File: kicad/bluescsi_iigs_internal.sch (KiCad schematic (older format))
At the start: 23 parts, among them J1 Conn_02x13_Odd_Even, J2 Conn_02x13_Odd_Even, J3 105162-0001, J4 Conn_01x02_Male, SW1 SW_SPDT, U1 YAAJ_BluePill, U2 UCC5606, U3 UCC5606, U4 AMS1117-5.0

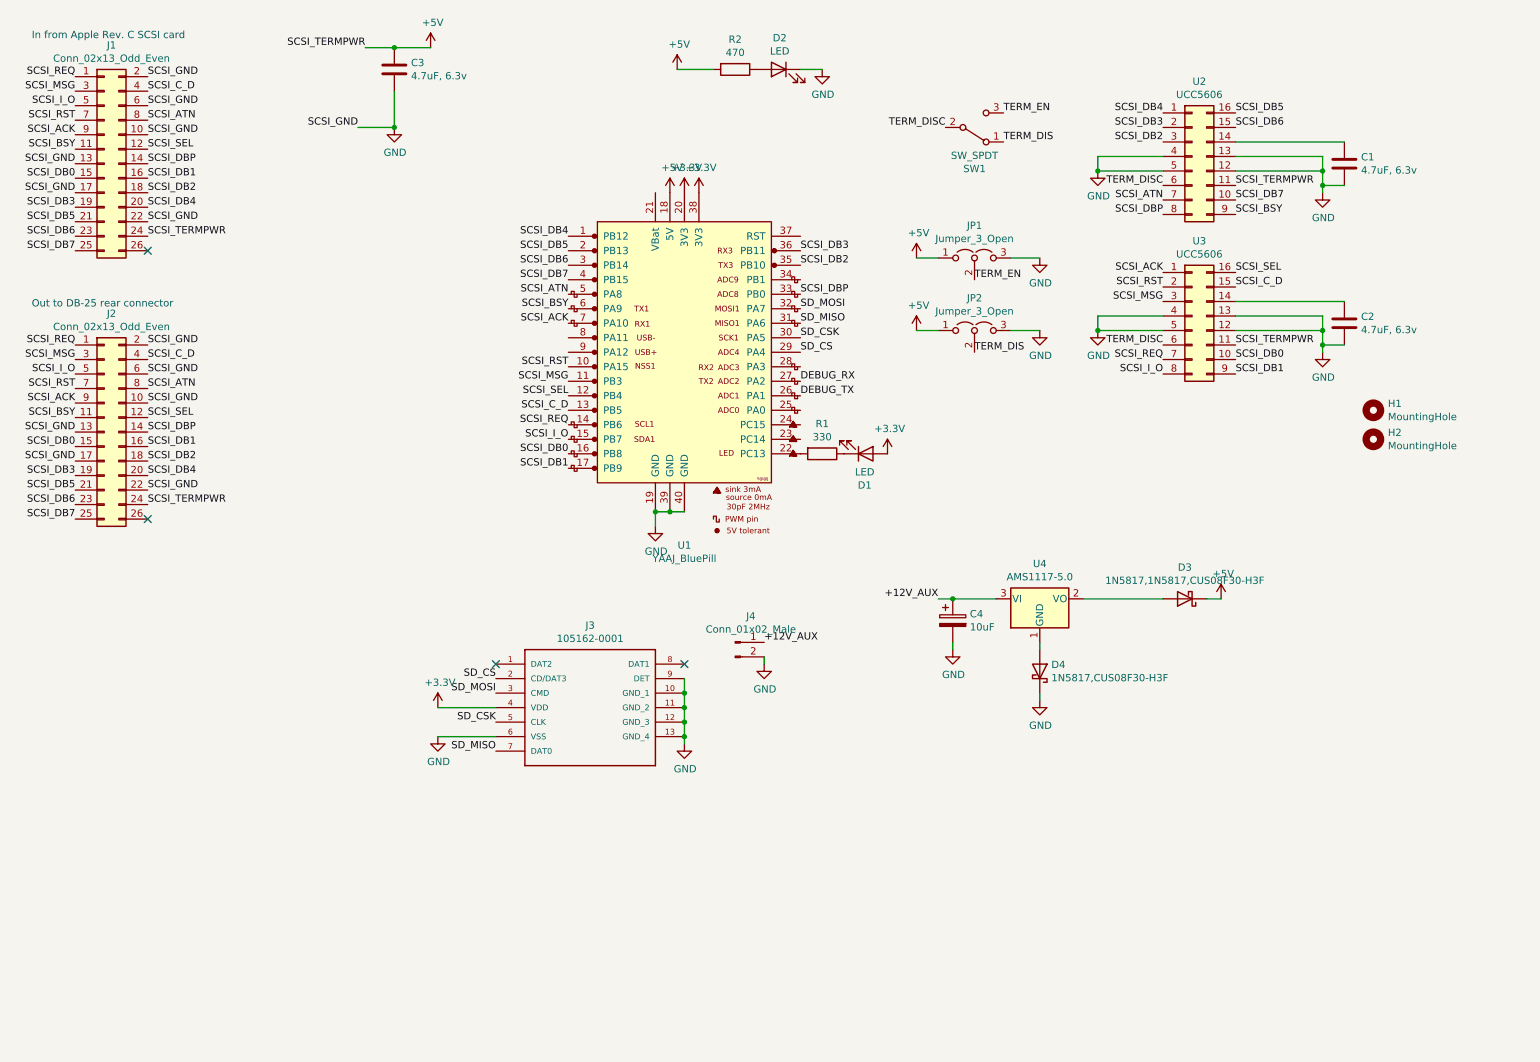
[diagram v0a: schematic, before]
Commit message: Updated schematic to group items and make them more readable
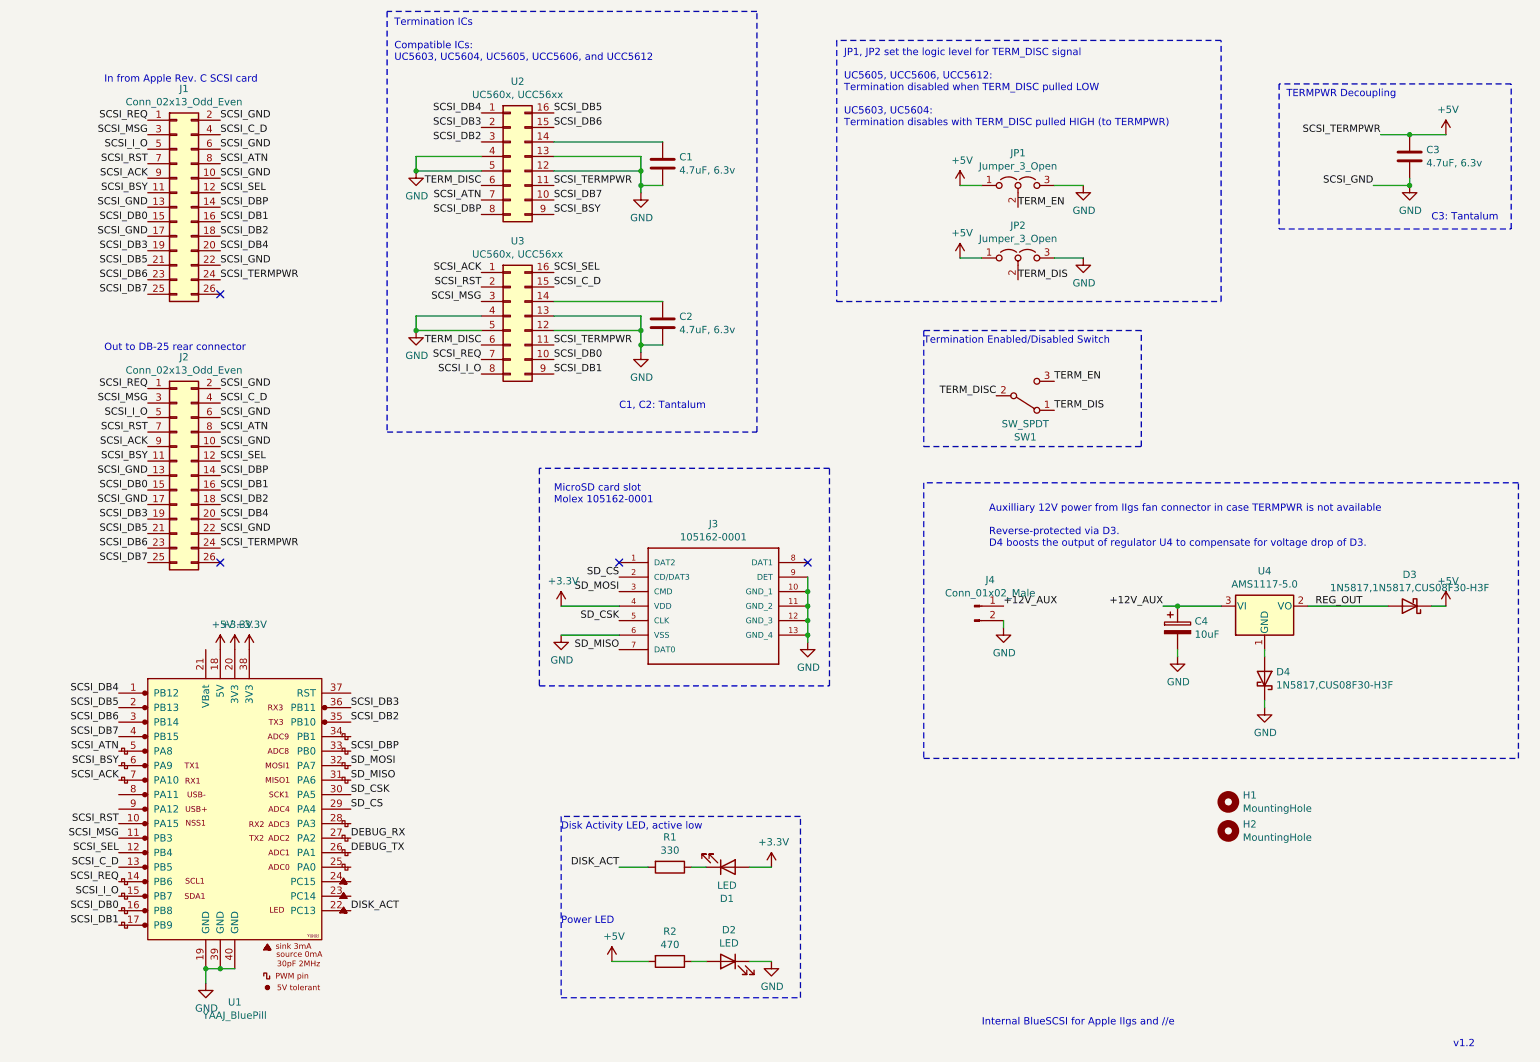
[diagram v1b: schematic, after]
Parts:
- U2, U3: value UCC5606 -> UC560x, UCC56xx
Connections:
- net DISK_ACT: now reaches R1.2, U1.22 (PC13)
- net REG_OUT: now reaches D3.2 (A), U4.2 (VO)
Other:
- note added: "Auxilliary 12V power from IIgs fan connector in case TERMPWR is not available\n\nReverse-protected via D3.\nD4 boosts the output of regulator U4 to compensate for voltage drop of D3."
- note added: "C1, C2: Tantalum"
- note added: "C3: Tantalum"
- note added: "Disk Activity LED, active low"
- note added: "Internal BlueSCSI for Apple IIgs and //e"
- note added: "JP1, JP2 set the logic level for TERM_DISC signal\n\nUC5605, UCC5606, UCC5612:\nTermination disabled when TERM_DISC pulled LOW\n\nUC5603, UC5604:\nTermination disables with TERM_DISC pulled HIGH (to TERMPWR)"
- note added: "MicroSD card slot\nMolex 105162-0001"
- note added: "Power LED"
- note added: "TERMPWR Decoupling"
- note added: "Termination Enabled/Disabled Switch"
- note added: "Termination ICs\n\nCompatible ICs:\nUC5603, UC5604, UC5605, UCC5606, and UCC5612"
- note added: "v1.2"
- moved on the sheet: C1, C2, C3, C4, D1, D2, D3, D4, H1, H2, J1, J2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

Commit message: Update notes about which JP setting to use with UCC5612
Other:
- note added: "JP1, JP2 set the logic level for TERM_DISC signal\n\nUC5605, UCC5606:\nTermination disabled when TERM_DISC pulled LOW\n\nUC5603, UC5604, UCC5612:\nTermination disables with TERM_DISC pulled HIGH (to TERMPWR)"
- note removed: "JP1, JP2 set the logic level for TERM_DISC signal\n\nUC5605, UCC5606, UCC5612:\nTermination disabled when TERM_DISC pulled LOW\n\nUC5603, UC5604:\nTermination disables with TERM_DISC pulled HIGH (to TERMPWR)"
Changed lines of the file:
@@
 Termination ICs\n\nCompatible ICs:\nUC5603, UC5604, UC5605, UCC5606, and UCC5612
 Text Notes 6400 1300 0    50   ~ 0
-JP1, JP2 set the logic level for TERM_DISC signal\n\nUC5605, UCC5606, UCC5612:\nTermination disabled when TERM_DISC pulled LOW\n\nUC5603, UC5604:\nTermination disables with TERM_DISC pulled HIGH (to TERMPWR)
+JP1, JP2 set the logic level for TERM_DISC signal\n\nUC5605, UCC5606:\nTermination disabled when TERM_DISC pulled LOW\n\nUC5603, UC5604, UCC5612:\nTermination disables with TERM_DISC pulled HIGH (to TERMPWR)
 Text Notes 6950 2800 0    50   ~ 0
 Termination Enabled/Disabled Switch

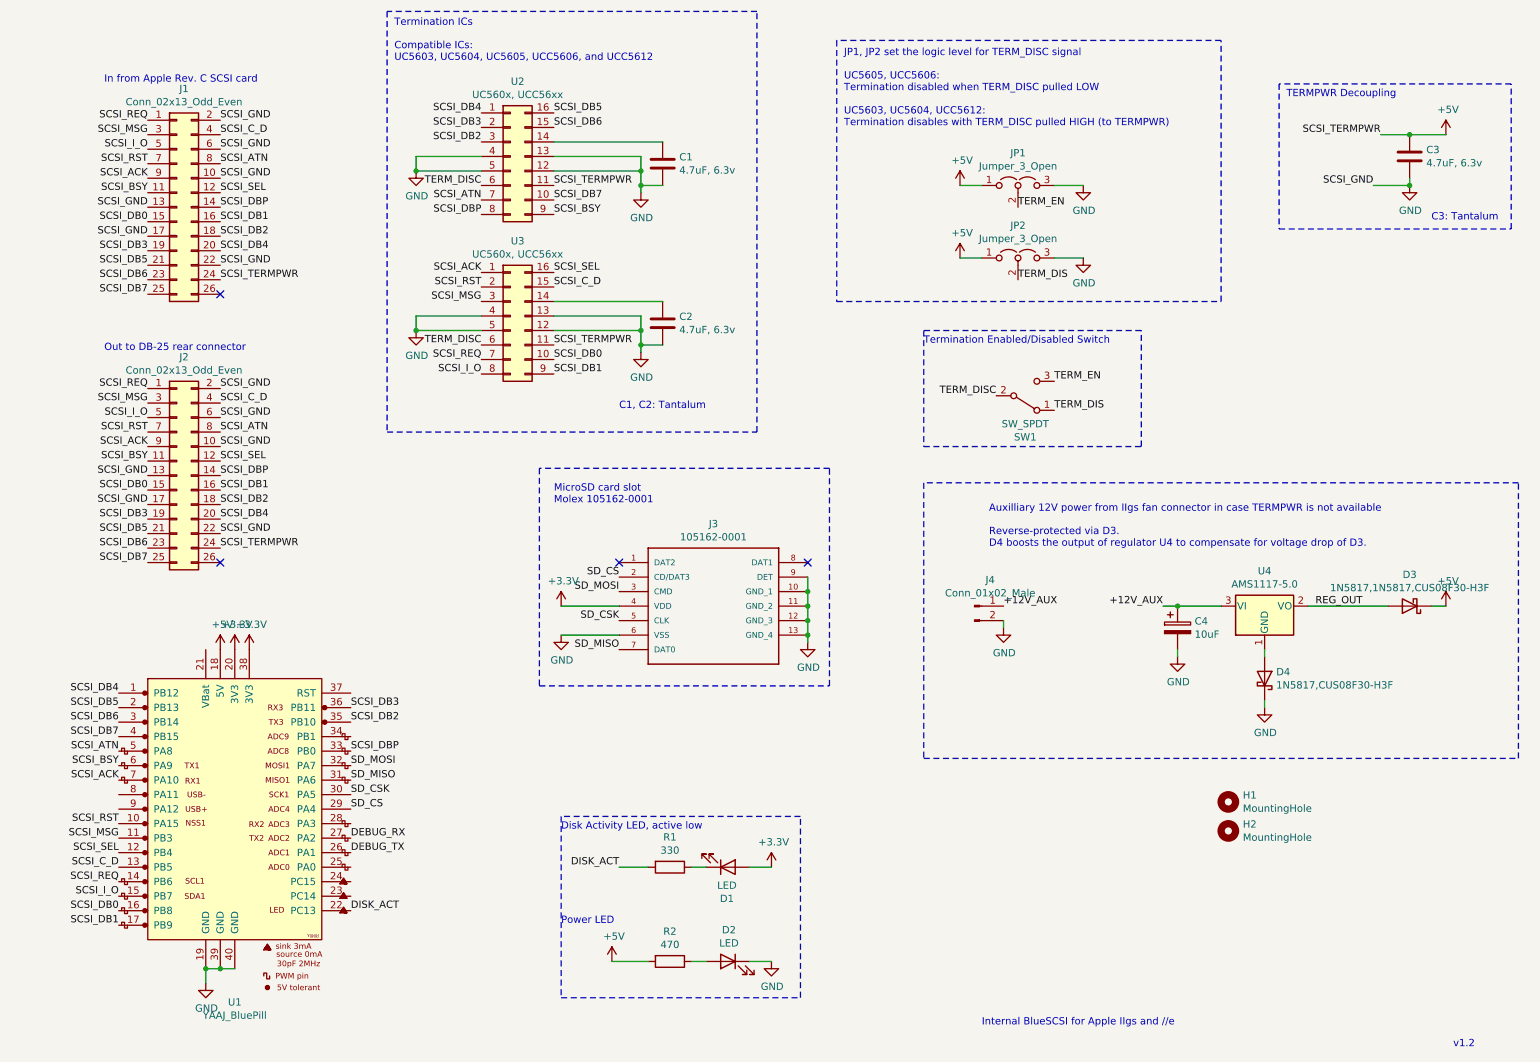
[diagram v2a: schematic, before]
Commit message: Add fuse
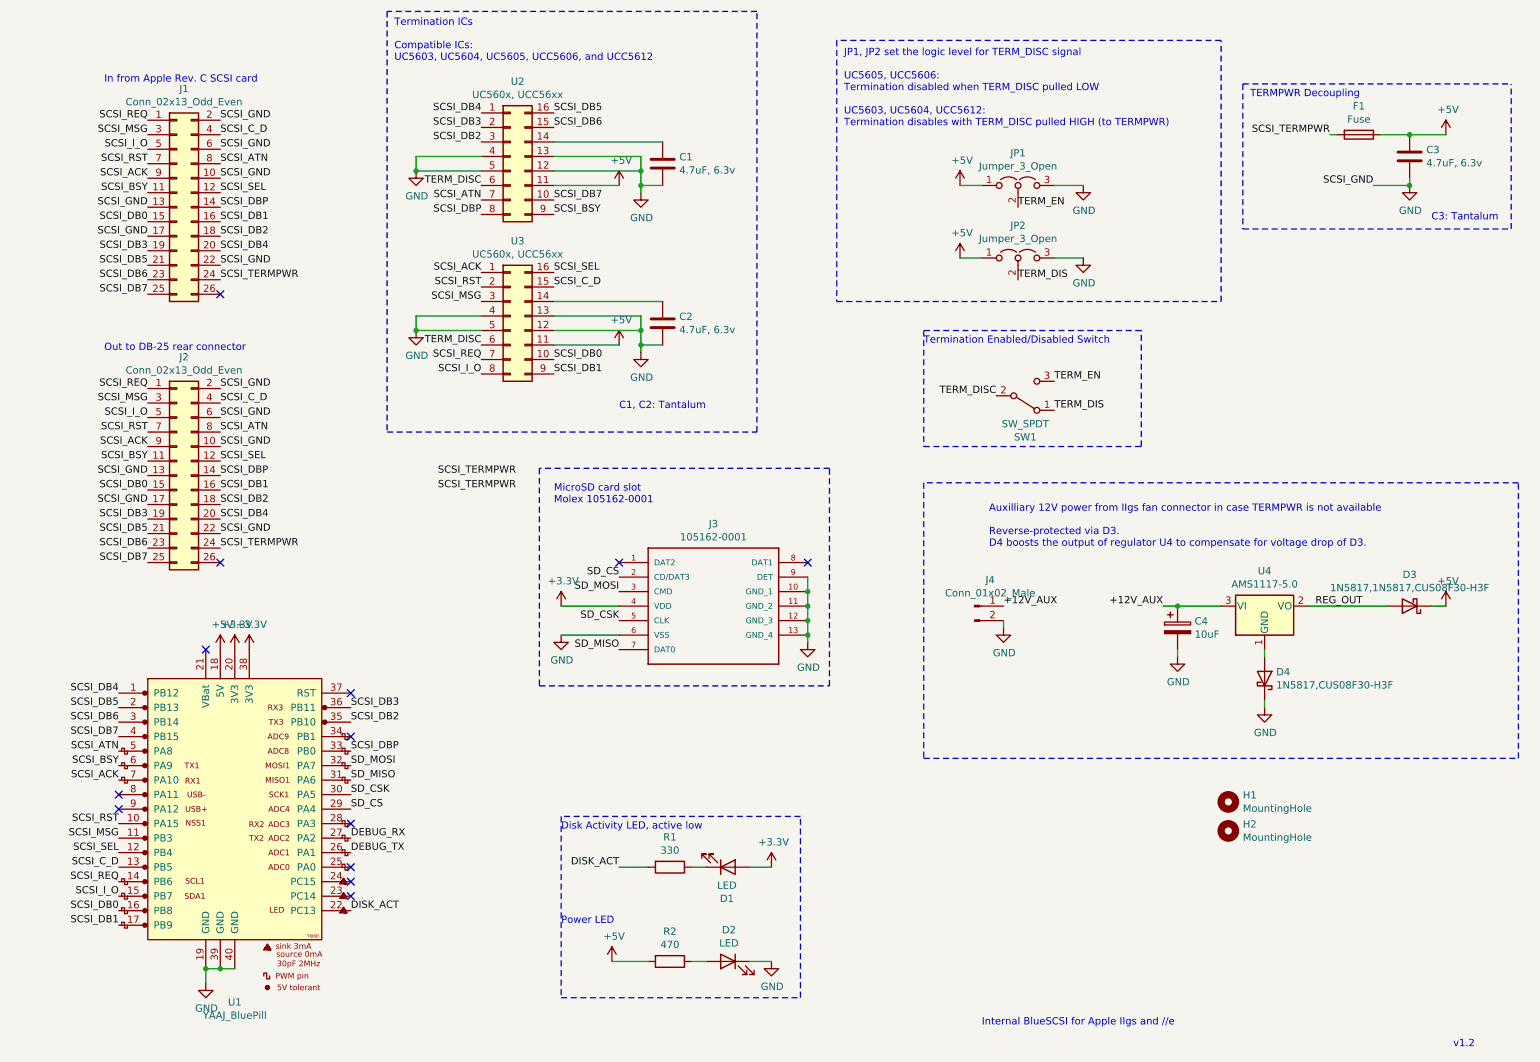
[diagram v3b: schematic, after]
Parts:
- added F1: Fuse, Fuse:Fuse_1210_3225Metric, symbol Device:Fuse
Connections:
- net +5V: now also F1.1; no longer J1.24 (Pin_24), J2.24 (Pin_24)
- new net SCSI_TERMPWR: F1.2, J1.24 (Pin_24), J2.24 (Pin_24)
- no-connect marks 4 -> 13
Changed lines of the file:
@@
 NoConn ~ 2100 2450
 NoConn ~ 2100 4300
-Text Label 10100 1350 2    50   ~ 0
-SCSI_TERMPWR
-$Comp
-L power:+5V #PWR0101
-U 1 1 606198ED
-P 10550 1350
-F 0 "#PWR0101" H 10550 1200 50  0001 C CNN
-F 1 "+5V" H 10565 1523 50  0000 C CNN
-F 2 "" H 10550 1350 50  0001 C CNN
-F 3 "" H 10550 1350 50  0001 C CNN
-	1    10550 1350
-	1    0    0    -1
-$EndComp
-$Comp
-L power:GND #PWR0102
-U 1 1 6061A0BF
-P 10300 1700
-F 0 "#PWR0102" H 10300 1450 50  0001 C CNN
-F 1 "GND" H 10305 1527 50  0000 C CNN
-F 2 "" H 10300 1700 50  0001 C CNN
-F 3 "" H 10300 1700 50  0001 C CNN
-	1    10300 1700
-	1    0    0    -1
-$EndComp
 $Comp
 L power:GND #PWR0103
@@
 	1    0    0    -1
 $EndComp
-Text Label 10050 1700 2    50   ~ 0
-SCSI_GND
 Wire Wire Line
 	2000 7100 2100 7100
@@
 	1    0    0    -1
 $EndComp
-Text Label 4400 1700 0    50   ~ 0
+Text Label 3600 3700 0    50   ~ 0
 SCSI_TERMPWR
 Wire Wire Line
@@
 	1    0    0    -1
 $EndComp
-Text Label 4400 2800 0    50   ~ 0
+Text Label 3600 3800 0    50   ~ 0
 SCSI_TERMPWR
 Wire Wire Line
@@
 	1    0    0    -1
 $EndComp
-$Comp
-L Device:C C3
-U 1 1 60643B6E
-P 10300 1500
-F 0 "C3" H 10415 1546 50  0000 L CNN
-F 1 "4.7uF, 6.3v" H 10415 1455 50  0000 L CNN
-F 2 "Capacitor_Tantalum_SMD:CP_EIA-3528-21_Kemet-B_Pad1.50x2.35mm_HandSolder" H 10338 1350 50  0001 C CNN
-F 3 "~" H 10300 1500 50  0001 C CNN
-	1    10300 1500
-	1    0    0    -1
-$EndComp
-Wire Wire Line
-	10300 1350 10550 1350
-Wire Wire Line
-	10100 1350 10300 1350
-Connection ~ 10300 1350
-Wire Wire Line
-	10050 1700 10300 1700
 Text Label 3000 6300 0    50   ~ 0
 DEBUG_TX
@@
 Wire Notes Line
 	5800 500  3250 500
-Connection ~ 10300 1700
-Wire Wire Line
-	10300 1700 10300 1650
-Text Notes 9450 1100 0    50   ~ 0
-TERMPWR Decoupling
+Text Label 9650 4600 0    50   ~ 0
+REG_OUT
+Wire Notes Line
+	9150 1000 11000 1000
+Wire Notes Line
+	9150 2000 11000 2000
+Wire Notes Line
+	9150 1000 9150 2000
 Text Notes 10450 1950 0    50   ~ 0
 C3: Tantalum
-Wire Notes Line
-	9400 1000 9400 2000
-Wire Notes Line
-	9400 2000 11000 2000
+Text Notes 9200 1100 0    50   ~ 0
+TERMPWR Decoupling
+Wire Wire Line
+	10300 1700 10300 1650
+Connection ~ 10300 1700
+Wire Wire Line
+	10050 1700 10300 1700
+Connection ~ 10300 1350
+Wire Wire Line
+	10100 1350 10300 1350
+Wire Wire Line
+	10300 1350 10550 1350
+$Comp
+L Device:C C3
+U 1 1 60643B6E
+P 10300 1500
+F 0 "C3" H 10415 1546 50  0000 L CNN
+F 1 "4.7uF, 6.3v" H 10415 1455 50  0000 L CNN
+F 2 "Capacitor_Tantalum_SMD:CP_EIA-3528-21_Kemet-B_Pad1.50x2.35mm_HandSolder" H 10338 1350 50  0001 C CNN
+F 3 "~" H 10300 1500 50  0001 C CNN
+	1    10300 1500
+	1    0    0    -1
+$EndComp
+Text Label 10050 1700 2    50   ~ 0
+SCSI_GND
+$Comp
+L power:GND #PWR0102
+U 1 1 6061A0BF
+P 10300 1700
+F 0 "#PWR0102" H 10300 1450 50  0001 C CNN
+F 1 "GND" H 10305 1527 50  0000 C CNN
+F 2 "" H 10300 1700 50  0001 C CNN
+F 3 "" H 10300 1700 50  0001 C CNN
+	1    10300 1700
+	1    0    0    -1
+$EndComp
+$Comp
+L power:+5V #PWR0101
+U 1 1 606198ED
+P 10550 1350
+F 0 "#PWR0101" H 10550 1200 50  0001 C CNN
+F 1 "+5V" H 10565 1523 50  0000 C CNN
+F 2 "" H 10550 1350 50  0001 C CNN
+F 3 "" H 10550 1350 50  0001 C CNN
+	1    10550 1350
+	1    0    0    -1
+$EndComp
+Wire Wire Line
+	9750 1350 9800 1350
+$Comp
+L Device:Fuse F1
+U 1 1 6099AB77
+P 9950 1350
+F 0 "F1" V 9753 1350 50  0000 C CNN
+F 1 "Fuse" V 9844 1350 50  0000 C CNN
+F 2 "Fuse:Fuse_1210_3225Metric" V 9880 1350 50  0001 C CNN
+F 3 "~" H 9950 1350 50  0001 C CNN
+	1    9950 1350
+	0    1    1    0
+$EndComp
+Text Label 9750 1350 2    50   ~ 0
+SCSI_TERMPWR
+NoConn ~ 2000 4900
+NoConn ~ 1400 5900
+NoConn ~ 1400 6000
+NoConn ~ 3000 6100
+NoConn ~ 3000 6400
+NoConn ~ 3000 6500
+NoConn ~ 3000 6600
+NoConn ~ 3000 5200
+NoConn ~ 3000 5500
 Wire Notes Line
 	11000 2000 11000 1000
-Wire Notes Line
-	11000 1000 9400 1000
-Text Label 9650 4600 0    50   ~ 0
-REG_OUT
+$Comp
+L power:+5V #PWR?
+U 1 1 609BE96D
+P 4850 2800
+F 0 "#PWR?" H 4850 2650 50  0001 C CNN
+F 1 "+5V" H 4865 2973 50  0000 C CNN
+F 2 "" H 4850 2800 50  0001 C CNN
+F 3 "" H 4850 2800 50  0001 C CNN
+	1    4850 2800
+	1    0    0    -1
+$EndComp
+$Comp
+L power:+5V #PWR?
+U 1 1 609BF84F
+P 4850 1700
+F 0 "#PWR?" H 4850 1550 50  0001 C CNN
+F 1 "+5V" H 4865 1873 50  0000 C CNN
+F 2 "" H 4850 1700 50  0001 C CNN
+F 3 "" H 4850 1700 50  0001 C CNN
+	1    4850 1700
+	1    0    0    -1
+$EndComp
+Wire Wire Line
+	4400 2800 4850 2800
+Wire Wire Line
+	4400 1700 4850 1700
 $EndSCHEMATC
